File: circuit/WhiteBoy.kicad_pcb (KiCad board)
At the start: 2 copper layers, 100 x 100 mm, 102 parts, among them J1 HOLE, J2 HOLE, J3 HOLE, J4 HOLE, Q1 IRF530NPbF, Q2 BC547, Q3 BC557, Q4 BC547, SW1 POS, SW2 NEG, T1 PB0, T2 PB1, T3 PB2, T4 PC1, T5 PC3, T6 PD6, T7 PD7, U1 74AC164, U10 74AC164, U11 CSR8635_MODULE, U12 TPA3136D2, U13 CSR_DebugSmall, U2 DS18B20, U3 MAX6457, U4 INA219_SOIC, U5 AVR-ISP6, U6 ATMEGA88PA-16AU, U7 74AC164, U8 DBG, U9 LM2576T-ADJ, Y1 16MHz

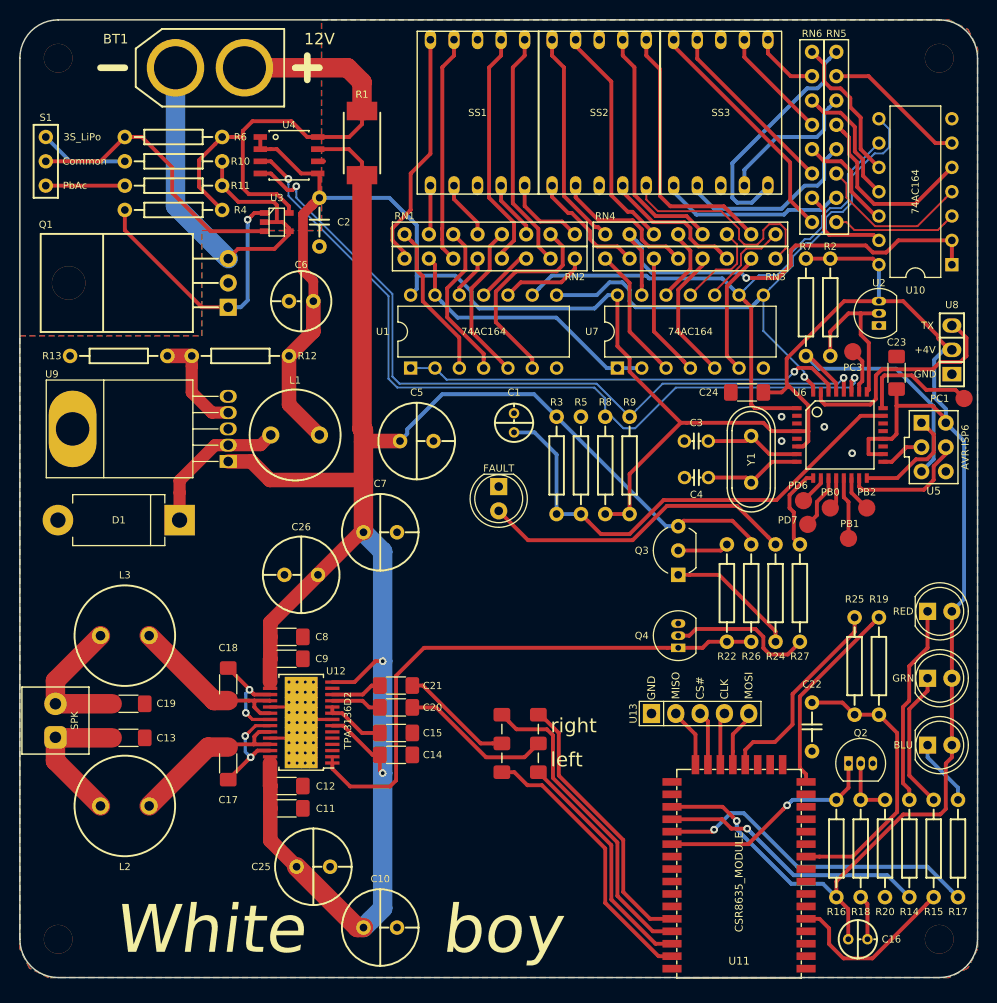
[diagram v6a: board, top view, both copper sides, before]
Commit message: Wpower and Wh displayed CSR8645 first draft
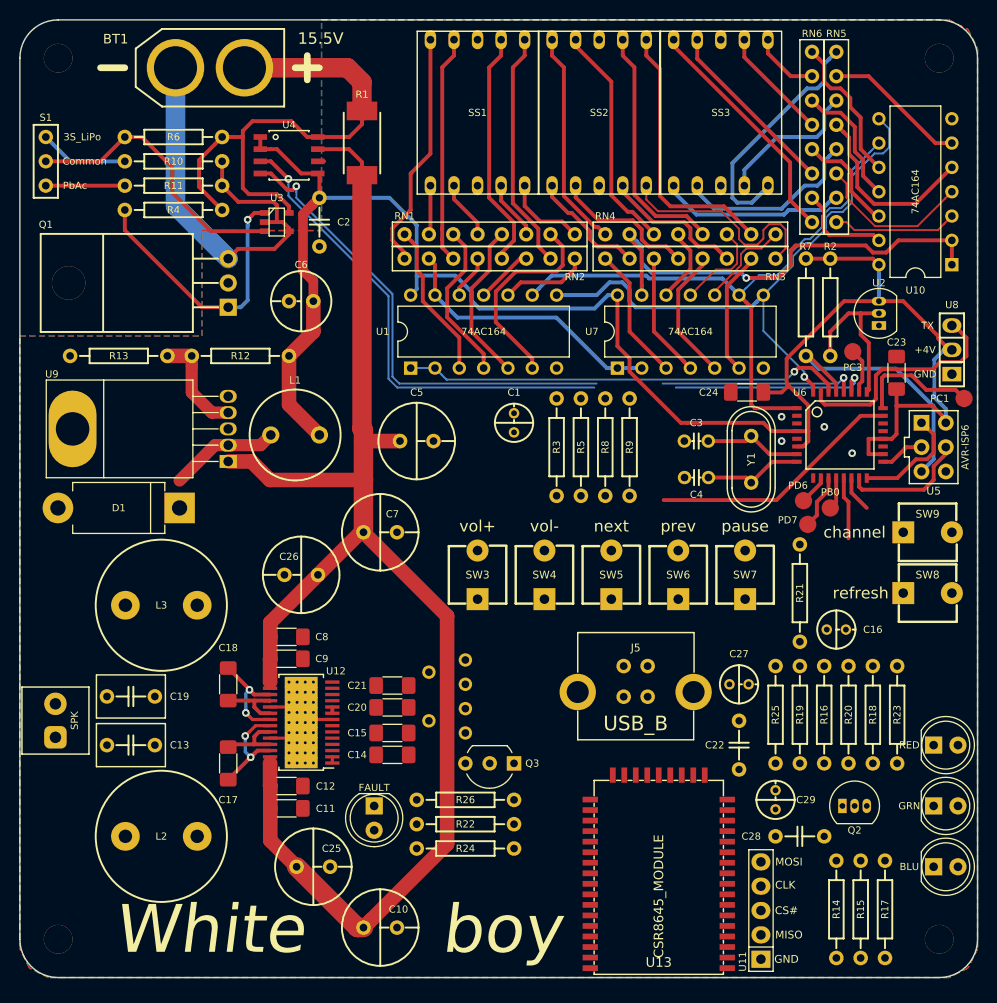
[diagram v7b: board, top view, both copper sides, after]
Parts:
- removed Q4: BC547, NovaBox:TO-92_Inline_Narrow_Oval
- removed R27: 1K, NovaBox:R_10MM
- removed T2: PB1, NovaBox:TestPad
- removed T3: PB2, NovaBox:TestPad
- added C27: 1uF, NovaBox:CPOL_D4_P2, F.Cu at (125.1, 119.4)
- added C28: 100nF, NovaBox:C_5MM, F.Cu at (131.4, 135.3)
- added C29: 1uF, NovaBox:CPOL_D4_P2, F.Cu at (128.9, 131.4)
- added J5: USB_B, NovaBox:USB_B_VERT, F.Cu at (114.3, 117.5)
- added R21: 470, NovaBox:R_10MM, F.Cu at (131.4, 109.9)
- added R23: 1K, NovaBox:R_10MM, F.Cu at (141.6, 122.6)
- added SW3: vol+, NovaBox:Tact_6x6, F.Cu at (97.8, 108.0)
- added SW4: vol-, NovaBox:Tact_6x6, F.Cu at (104.8, 108.0)
- added SW5: next, NovaBox:Tact_6x6, F.Cu at (111.8, 108.0)
- added SW6: prev, NovaBox:Tact_6x6, F.Cu at (118.7, 108.0)
- added SW7: pause, NovaBox:Tact_6x6, F.Cu at (125.7, 108.0)
- added SW8: refresh, NovaBox:Tact_6x6, F.Cu at (144.8, 109.9)
- added SW9: channel, NovaBox:Tact_6x6, F.Cu at (144.8, 103.5)
- BT1: value 12V -> 15.5V
- C13, C19: footprint NovaBox:C_1206 -> NovaBox:C_FILM_5MM
- L2, L3: footprint NovaBox:COIL_DR0810 -> NovaBox:COILCRAFT_RFS1412
- U11: value CSR8635_MODULE -> CSR_CFG; footprint NovaBox:CSR8635_MODULE -> NovaBox:CSR_DebugSmall
- U13: value CSR_DebugSmall -> CSR8645_MODULE; footprint NovaBox:CSR_DebugSmall -> NovaBox:CSR8645_MODULE
- moved R24 42.0 mm to (96.5, 136.5), turned to 180 degrees
- moved R26 36.8 mm to (96.5, 131.4), turned to 180 degrees
- moved R22 36.4 mm to (96.5, 134.0), turned to 0 degrees
- moved D5 35.8 mm to (87.0, 133.3)
- moved C16 32.4 mm to (135.3, 113.7)
- moved Q3 29.7 mm to (99.1, 127.6), turned to 180 degrees
- moved U11 14.9 mm to (127.4, 143.0), turned to 90 degrees
- moved R20 14.5 mm to (136.5, 122.6), turned to 270 degrees
- moved R18 14.0 mm to (139.1, 122.6), turned to 90 degrees
- moved R16 14.0 mm to (134.0, 122.6), turned to 90 degrees
- moved D2 14.0 mm to (146.7, 125.7)
- moved D3 13.4 mm to (146.7, 132.1)
- moved D4 12.7 mm to (146.7, 138.4)
- moved SW2 11.7 mm to (92.7, 123.2), turned to 0 degrees
- moved SW1 10.7 mm to (92.7, 118.1), turned to 0 degrees
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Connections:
- net Net-(Q4-Pad1) renamed /SD_FAULT
- Q2 pad 1: /MFB -> /PWER_E
- R14 pad 1: LED_R -> Net-(R14-Pad1)
- R15 pad 1: LED_G -> Net-(R15-Pad1)
- R16 pad 1: /MFB -> /PWER_E
- R17 pad 1: LED_B -> Net-(R17-Pad1)
- R19 pad 2: Net-(R19-Pad2) -> /SPI_PCM
- U11 pad 1: (no net) -> Net-(U11-Pad1)
- U11 pad 2: (no net) -> Net-(U11-Pad2)
- U11 pad 3: (no net) -> Net-(U11-Pad3)
- U11 pad 4: (no net) -> Net-(U11-Pad4)
- U11 pad 5: LED_G -> GND
- U13 pad 1: Net-(U11-Pad21) -> Net-(R17-Pad1)
- U13 pad 2: Net-(U11-Pad22) -> Net-(R15-Pad1)
- U13 pad 3: Net-(U11-Pad23) -> Net-(R14-Pad1)
- U13 pad 4: Net-(U11-Pad24) -> (no net)
- U13 pad 5: GND -> Net-(U11-Pad4)
- U6 pad 9: AMP_SHDN -> (no net)
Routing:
- net +4V: track 284.3 -> 185.4 mm, vias 1 -> 0
- net /SD_FAULT: track 58.4 -> 0.65 mm
- net VDD: track 207.6 -> 152.5 mm, vias 2 -> 0
- net LED_B: track 34.3 -> 0.00 mm, vias 1 -> 0
- net Net-(D5-Pad2): track 33.3 -> 0.00 mm
- net /SPK_RP: track 33.0 -> 0.00 mm
- net 1V8: track 29.9 -> 0.00 mm
- net /SPK_LP: track 29.1 -> 0.00 mm
- net /SPK_RN: track 28.6 -> 0.00 mm
- net LED_R: track 28.1 -> 0.00 mm, vias 1 -> 0
- net BATT_SNS: track 51.7 -> 26.6 mm
- net /SPK_LN: track 24.7 -> 0.00 mm
- net /MFB: track 23.4 -> 0.00 mm, vias 1 -> 0
- net Net-(R25-Pad2): track 21.4 -> 0.00 mm
- net Net-(D2-Pad1): track 21.0 -> 0.00 mm
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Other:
- board text removed: "left"
- board text removed: "right"

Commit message: finished first draft PCB
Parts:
- removed D3: GRN, NovaBox:LED_D5.0mm
- removed D4: BLU, NovaBox:LED_D5.0mm
- D2: value RED -> LED_RCBG; footprint NovaBox:LED_D5.0mm -> NovaBox:LED_RCBG
- moved Q2 12.6 mm to (145.4, 122.6), turned to 270 degrees
- moved D2 10.8 mm to (138.4, 132.7)
- moved C20 0.13 mm to (88.9, 121.9)
- moved C21 0.13 mm to (88.9, 119.6)
- moved SW1 0.13 mm to (92.7, 118.2)
- moved SW2 0.13 mm to (92.7, 123.3)
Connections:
- net Net-(C17-Pad1) renamed /OUTL
- net Net-(C18-Pad1) renamed /OUTR
- R14 pad 2: Net-(D2-Pad1) -> Net-(D2-PadGA)
- R15 pad 2: Net-(D3-Pad1) -> Net-(D2-PadBA)
- R17 pad 2: Net-(D4-Pad1) -> Net-(D2-PadRA)
- SW1 pad 1: /SPK_LP -> /SPK_LN
- SW1 pad 3: /SPK_RP -> /SPK_RN
- SW2 pad 1: /SPK_LN -> /SPK_LP
- SW2 pad 3: /SPK_RN -> /SPK_RP
- U13 pad 1: Net-(R17-Pad1) -> Net-(R14-Pad1)
- U13 pad 3: Net-(R14-Pad1) -> Net-(R17-Pad1)
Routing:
- net +4V: track 185.4 -> 286.2 mm
- net VDD: track 152.5 -> 205.0 mm
- net /PAUSE: track 0.00 -> 42.3 mm
- net /PREV: track 0.00 -> 36.2 mm
- net VBUS: track 0.00 -> 35.2 mm
- net /SPK_LN: track 0.00 -> 34.7 mm
- net Net-(R21-Pad2): track 0.00 -> 33.9 mm
- net /VOL+: track 0.00 -> 32.9 mm
- net /SPK_RN: track 0.00 -> 32.7 mm
- net /NEXT: track 0.00 -> 30.9 mm
- net /PWER_E: track 0.00 -> 30.4 mm
- net /VOL-: track 0.00 -> 29.5 mm
- net /SPK_LP: track 0.00 -> 29.4 mm
- net /SPK_RP: track 0.00 -> 29.3 mm
- net 1V8: track 0.00 -> 23.8 mm
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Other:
- board text added: "white"
- board text removed: "White"
